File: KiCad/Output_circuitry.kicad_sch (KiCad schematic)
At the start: 13 parts, among them IC1 TPS63070RNMR, IC2 ISL23511WFB8Z

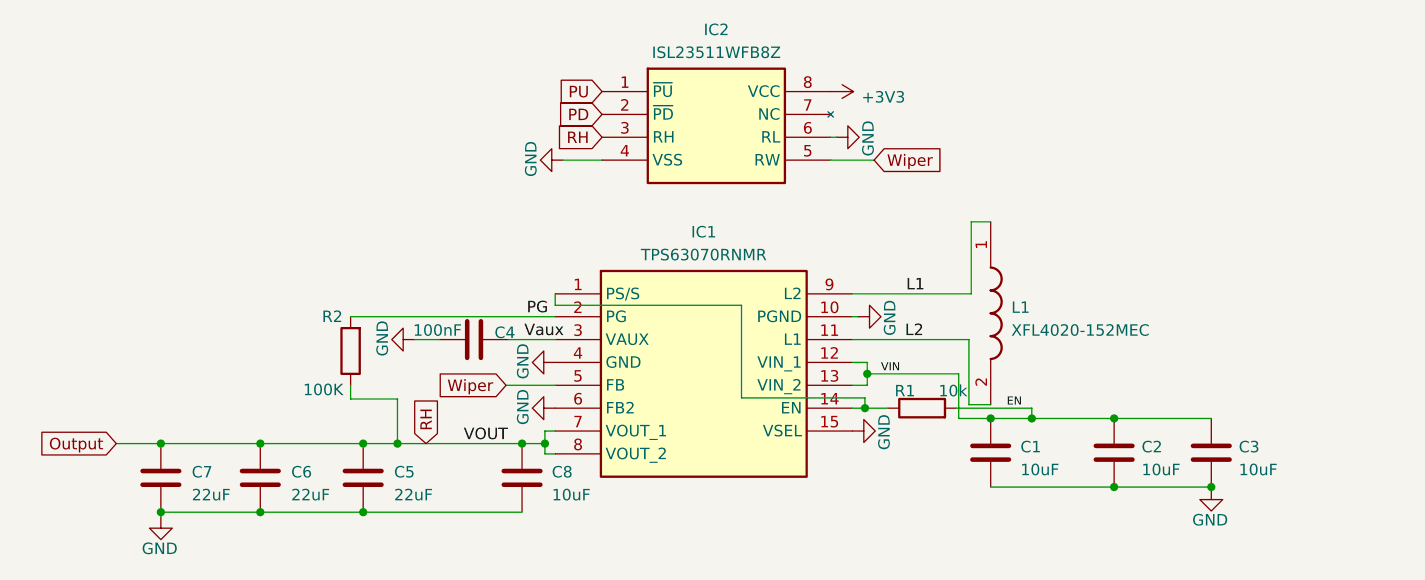
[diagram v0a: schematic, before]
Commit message: Schematic redesign needs two footprints before complete.
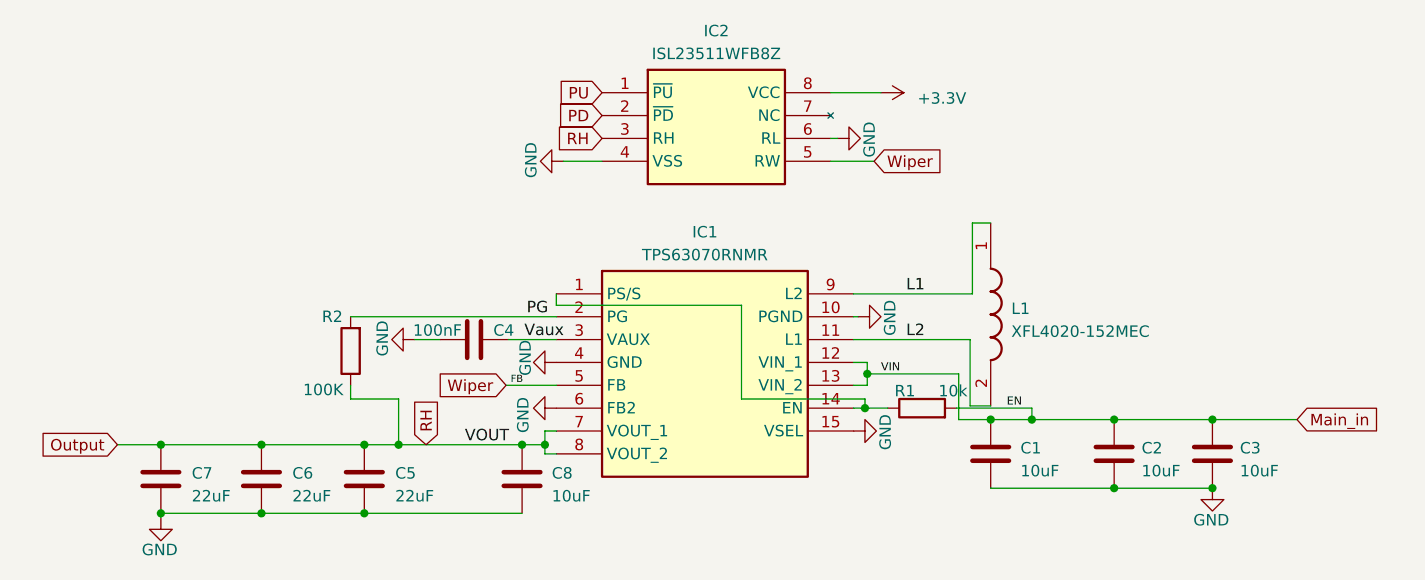
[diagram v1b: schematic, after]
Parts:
- IC1: footprint TPS630701RNMR -> Custom_eric:TPS630701RNMR
- IC2: footprint SOIC127P600X175-8N -> Custom_eric:SOIC127P600X175-8N
- L1: footprint XFL4020152MEC -> Custom_eric:XFL4020152MEC
- R1: footprint (none) -> Resistor_SMD:R_0402_1005Metric_Pad0.72x0.64mm_HandSolder
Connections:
- net +3V3 renamed +3.3V
- net EN renamed Main_in

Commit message: Board layout preleminary complete.
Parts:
- C1: footprint Capacitor_SMD:C_0603_1608Metric_Pad1.08x0.95mm_HandSolder -> Capacitor_SMD:C_0805_2012Metric_Pad1.18x1.45mm_HandSolder
- IC2: footprint Custom_eric:SOIC127P600X175-8N -> Custom_eric:ISL23511WFB8Z
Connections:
- net EN: now reaches IC1.1 (PS/S), IC1.14 (EN), R1.1
- net Output renamed ADC
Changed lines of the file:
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@@
     (stroke (width 0) (type default))
   )
-  (wire (pts (xy 76.708 93.98) (xy 71.882 93.98))
+  (wire (pts (xy 76.708 93.98) (xy 68.326 93.98))
     (stroke (width 0) (type default))
   )
@@
     (effects (font (size 1.27 1.27)) (justify left bottom))
   )
-  (label "EN" (at 170.688 89.916 0) (fields_autoplaced)
+  (label "L1" (at 159.512 77.216 0) (fields_autoplaced)
+    (effects (font (size 1.27 1.27)) (justify left bottom))
+  )
+  (label "EN" (at 156.21 89.916 0) (fields_autoplaced)
     (effects (font (size 0.9 0.9)) (justify left bottom))
-  )
-  (label "L1" (at 159.512 77.216 0) (fields_autoplaced)
-    (effects (font (size 1.27 1.27)) (justify left bottom))
   )
   (label "Vaux" (at 117.094 82.296 0) (fields_autoplaced)
@@
     )
   )
-  (global_label "Output" (shape input) (at 71.882 93.98 180) (fields_autoplaced)
-    (effects (font (size 1.27 1.27)) (justify right))
-    (property "Intersheetrefs" "${INTERSHEET_REFS}" (at 62.7473 93.98 0)
+  (global_label "ADC" (shape input) (at 79.629 93.98 90) (fields_autoplaced)
+    (effects (font (size 1.27 1.27)) (justify left))
+    (property "Intersheetrefs" "${INTERSHEET_REFS}" (at 79.629 87.4456 90)
+      (effects (font (size 1.27 1.27)) (justify left) hide)
+    )
+  )
+  (global_label "Output" (shape input) (at 68.326 93.98 180) (fields_autoplaced)
+    (effects (font (size 1.27 1.27)) (justify right))
+    (property "Intersheetrefs" "${INTERSHEET_REFS}" (at 59.1913 93.98 0)
       (effects (font (size 1.27 1.27)) (justify right) hide)
     )
@@
       (effects (font (size 1.27 1.27)) (justify left))
     )
-    (property "Footprint" "Capacitor_SMD:C_0603_1608Metric_Pad1.08x0.95mm_HandSolder" (at 169.8752 98.806 0)
+    (property "Footprint" "Capacitor_SMD:C_0805_2012Metric_Pad1.18x1.45mm_HandSolder" (at 169.8752 98.806 0)
       (effects (font (size 1.27 1.27)) hide)
     )
@@
       (effects (font (size 1.27 1.27)))
     )
-    (property "Footprint" "Custom_eric:SOIC127P600X175-8N" (at 147.32 149.784 0)
-      (effects (font (size 1.27 1.27)) (justify left top) hide)
-    )
+    (property "Footprint" "Custom_eric:ISL23511WFB8Z" (at 147.32 149.784 0)
+      (effects (font (size 1.27 1.27)) (justify left top) hide)
+    )

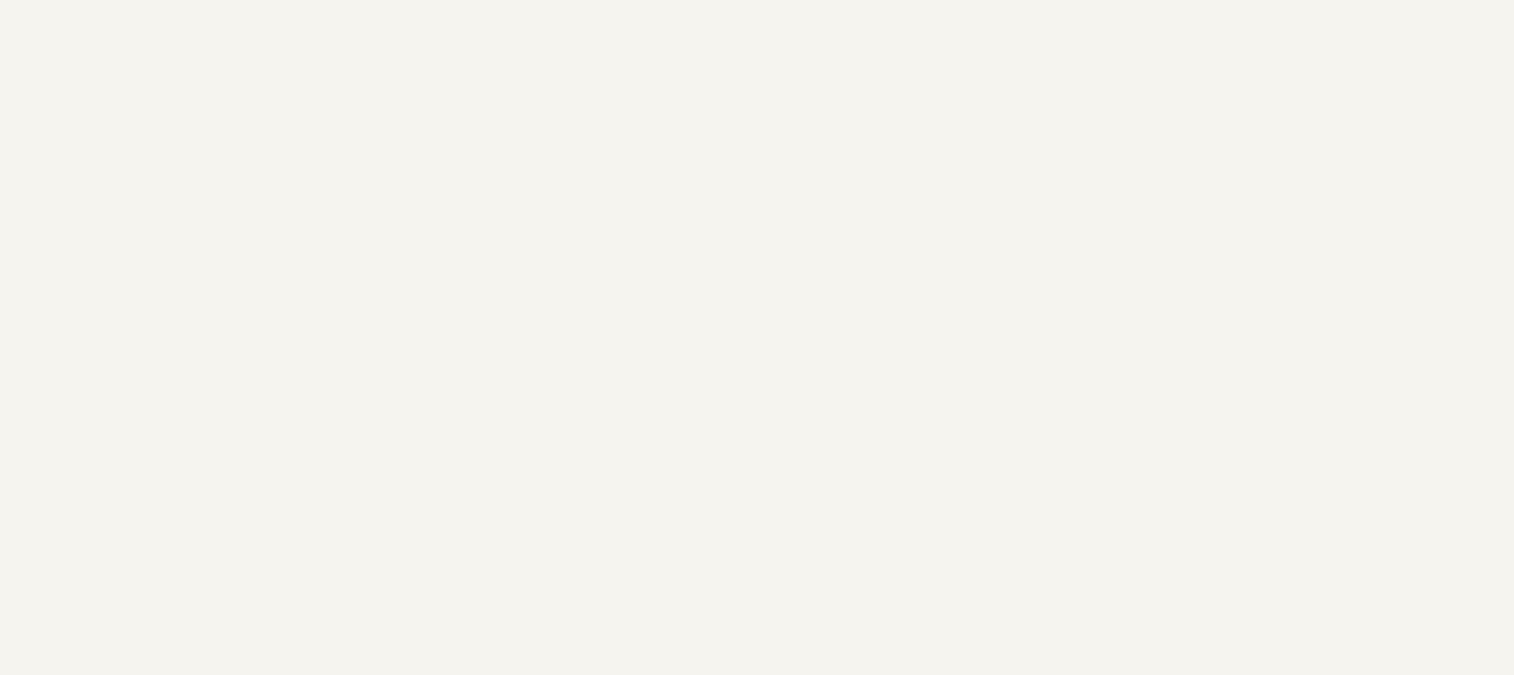
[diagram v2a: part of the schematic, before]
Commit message: Added some notes and extra ground vias.
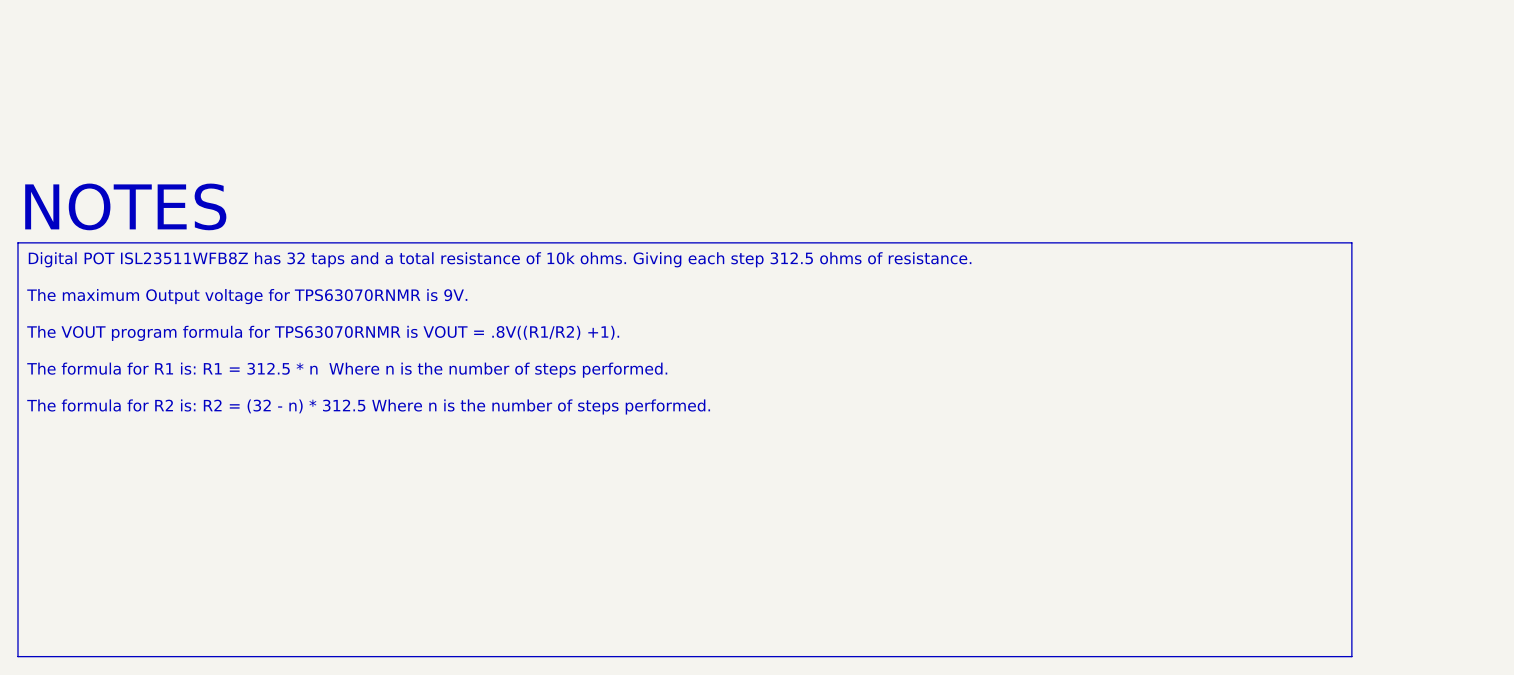
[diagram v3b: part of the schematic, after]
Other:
- note added: "NOTES"
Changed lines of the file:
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@@
     (stroke (width 0) (type default))
+  )
+  (text_box "Digital POT ISL23511WFB8Z has 32 taps and a total resistance of 10k ohms. Giving each step 312.5 ohms of resistance.\n\nThe maximum Output voltage for TPS63070RNMR is 9V.\n\nThe VOUT program formula for TPS63070RNMR is VOUT = .8V((R1/R2) +1).\n\nThe formula for R1 is: R1 = 312.5 * n  Where n is the number of steps performed.\n\nThe formula for R2 is: R2 = (32 - n) * 312.5 Where n is the number of steps performed."
+    (at 14.097 149.479 0) (size 148.209 45.974)
+    (stroke (width 0) (type default))
+    (fill (type none))
+    (effects (font (size 1.27 1.27)) (justify left top))
+  )
+  (text "NOTES" (at 14.224 148.844 0)
+    (effects (font (size 5 5)) (justify left bottom))
   )
   (label "PG" (at 117.348 79.756 0) (fields_autoplaced)

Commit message: Starting revision 1.1
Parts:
- C8: footprint Capacitor_SMD:C_0603_1608Metric_Pad1.08x0.95mm_HandSolder -> Capacitor_SMD:C_0805_2012Metric_Pad1.18x1.45mm_HandSolder
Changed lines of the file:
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@@
     (stroke (width 0) (type default))
   )
-  (wire (pts (xy 166.624 89.662) (xy 166.624 82.296))
+  (wire (pts (xy 166.624 89.408) (xy 166.624 82.296))
     (stroke (width 0) (type default))
   )
@@
     (stroke (width 0) (type default))
   )
-  (wire (pts (xy 166.878 77.216) (xy 166.878 69.342))
+  (wire (pts (xy 166.878 77.216) (xy 166.878 69.088))
     (stroke (width 0) (type default))
   )
@@
     (stroke (width 0) (type default))
   )
-  (wire (pts (xy 166.624 89.662) (xy 168.91 89.662))
+  (wire (pts (xy 166.624 89.408) (xy 168.91 89.408))
     (stroke (width 0) (type default))
   )
@@
     (stroke (width 0) (type default))
   )
-  (wire (pts (xy 166.878 69.342) (xy 168.91 69.342))
+  (wire (pts (xy 166.878 69.088) (xy 168.91 69.088))
     (stroke (width 0) (type default))
   )
@@
     (stroke (width 0) (type default))
   )
-  (text_box "Digital POT ISL23511WFB8Z has 32 taps and a total resistance of 10k ohms. Giving each step 312.5 ohms of resistance.\n\nThe maximum Output voltage for TPS63070RNMR is 9V.\n\nThe VOUT program formula for TPS63070RNMR is VOUT = .8V((R1/R2) +1).\n\nThe formula for R1 is: R1 = 312.5 * n  Where n is the number of steps performed.\n\nThe formula for R2 is: R2 = (32 - n) * 312.5 Where n is the number of steps performed."
+  (text_box "Digital POT ISL23511WFB8Z has 32 taps and a total resistance of 10k ohms. Giving each step 312.5 ohms of resistance.\n\nThe maximum Output voltage for TPS63070RNMR is 9V.\n\nThe VOUT program formula for TPS63070RNMR is VOUT = .8V((R1/R2) +1).\n\nThe formula for R1 is: R1 = 312.5 * n  \n\nThe formula for R2 is: R2 = (32 - n) * 312.5 \nWhere n is the number of steps performed and n <= 31.\n"
     (at 14.097 149.479 0) (size 148.209 45.974)
     (stroke (width 0) (type default))
@@
       (effects (font (size 1.27 1.27)) (justify left))
     )
-    (property "Footprint" "Capacitor_SMD:C_0603_1608Metric_Pad1.08x0.95mm_HandSolder" (at 117.8052 101.6 0)
+    (property "Footprint" "Capacitor_SMD:C_0805_2012Metric_Pad1.18x1.45mm_HandSolder" (at 117.8052 101.6 0)
       (effects (font (size 1.27 1.27)) hide)
     )
@@
     )
   )
-  (symbol (lib_id "Custom_eric:XFL4020-152MEC") (at 168.91 69.342 270) (unit 1)
-    (in_bom yes) (on_board yes) (dnp no) (fields_autoplaced)
-    (property "Reference" "L1" (at 171.196 78.867 90)
-      (effects (font (size 1.27 1.27)) (justify left))
-    )
-    (property "Value" "XFL4020-152MEC" (at 171.196 81.407 90)
-      (effects (font (size 1.27 1.27)) (justify left))
-    )
-    (property "Footprint" "Custom_eric:XFL4020152MEC" (at 72.72 85.852 0)
-      (effects (font (size 1.27 1.27)) (justify left top) hide)
-    )
-    (property "Datasheet" "https://www.coilcraft.com/getmedia/50632d43-da1b-4cdb-8ab4-3029cab51df3/xfl4020.pdf" (at -27.28 85.852 0)
-      (effects (font (size 1.27 1.27)) (justify left top) hide)
-    )
-    (property "Height" "2.1" (at -227.28 85.852 0)
-      (effects (font (size 1.27 1.27)) (justify left top) hide)
-    )
-    (property "Mouser Part Number" "994-XFL4020-152MEC" (at -327.28 85.852 0)
-      (effects (font (size 1.27 1.27)) (justify left top) hide)
-    )
-    (property "Mouser Price/Stock" "https://www.mouser.co.uk/ProductDetail/Coilcraft/XFL4020-152MEC?qs=zCSbvcPd3pak5QYA2uujRA%3D%3D" (at -427.28 85.852 0)
-      (effects (font (size 1.27 1.27)) (justify left top) hide)
-    )
-    (property "Manufacturer_Name" "COILCRAFT" (at -527.28 85.852 0)
-      (effects (font (size 1.27 1.27)) (justify left top) hide)
-    )
-    (property "Manufacturer_Part_Number" "XFL4020-152MEC" (at -627.28 85.852 0)
-      (effects (font (size 1.27 1.27)) (justify left top) hide)
-    )
+  (symbol (lib_id "Custom_eric:XFL4020-152MEC") (at 168.91 69.088 270) (unit 1)
+    (in_bom yes) (on_board yes) (dnp no) (fields_autoplaced)
+    (property "Reference" "L1" (at 171.196 78.613 90)
+      (effects (font (size 1.27 1.27)) (justify left))
+    )
+    (property "Value" "XFL4020-152MEC" (at 171.196 81.153 90)
+      (effects (font (size 1.27 1.27)) (justify left))
+    )
+    (property "Footprint" "Custom_eric:XFL4020152MEC" (at 72.72 85.598 0)
+      (effects (font (size 1.27 1.27)) (justify left top) hide)
+    )
+    (property "Datasheet" "https://www.coilcraft.com/getmedia/50632d43-da1b-4cdb-8ab4-3029cab51df3/xfl4020.pdf" (at -27.28 85.598 0)
+      (effects (font (size 1.27 1.27)) (justify left top) hide)
+    )
+    (property "Height" "2.1" (at -227.28 85.598 0)
+      (effects (font (size 1.27 1.27)) (justify left top) hide)
+    )
+    (property "Mouser Part Number" "994-XFL4020-152MEC" (at -327.28 85.598 0)
+      (effects (font (size 1.27 1.27)) (justify left top) hide)
+    )
+    (property "Mouser Price/Stock" "https://www.mouser.co.uk/ProductDetail/Coilcraft/XFL4020-152MEC?qs=zCSbvcPd3pak5QYA2uujRA%3D%3D" (at -427.28 85.598 0)
+      (effects (font (size 1.27 1.27)) (justify left top) hide)
+    )
+    (property "Manufacturer_Name" "COILCRAFT" (at -527.28 85.598 0)
+      (effects (font (size 1.27 1.27)) (justify left top) hide)
+    )
+    (property "Manufacturer_Part_Number" "XFL4020-152MEC" (at -627.28 85.598 0)
+      (effects (font (size 1.27 1.27)) (justify left top) hide)
+    )
